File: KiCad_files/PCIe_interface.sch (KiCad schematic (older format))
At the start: 13 parts, among them J1 PCIe_x4_Connector, U1 XC7A35T_CSG325

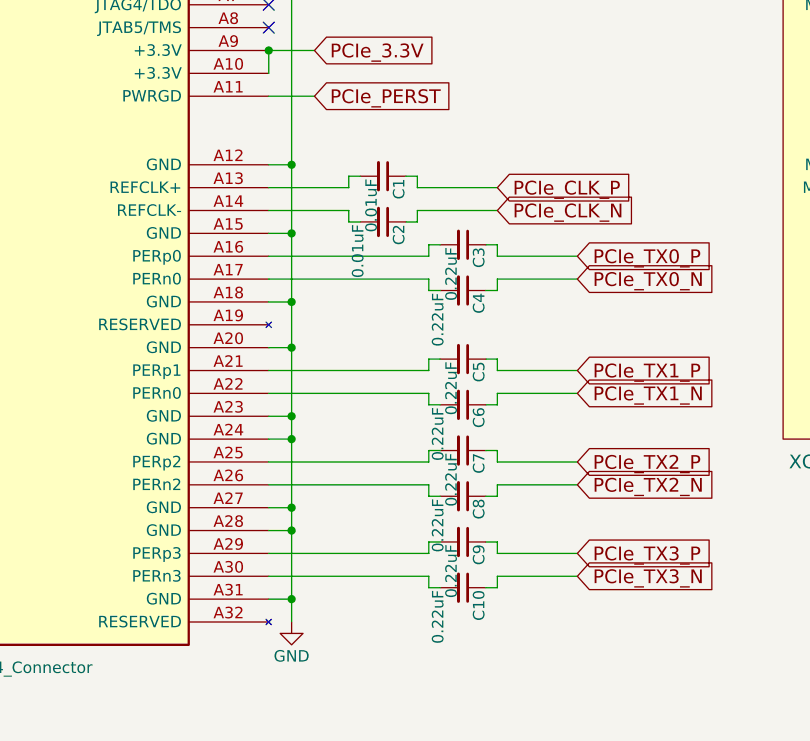
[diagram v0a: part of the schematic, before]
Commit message: Fixes during layout
Changed FT2232HL footprint to one with external pad
Made LGA123 (PI34XX) pins into blocks
Added labels for PCIe to let KiCad do differential pair routing
Removed some ground connections in SGND in PI34XX
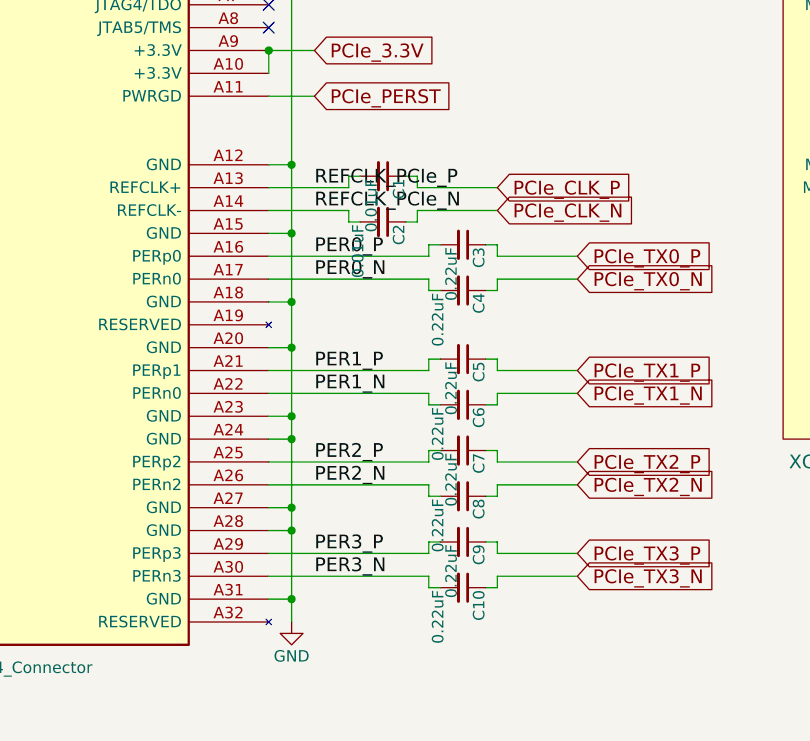
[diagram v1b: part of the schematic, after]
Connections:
- net REFCLK_PCIe_P: now reaches C1.2, J1.A13 (REFCLK+)
- net REFCLK_PCIe_N: now reaches C2.2, J1.A14 (REFCLK-)
- net PER0_P: now reaches C3.2, J1.A16 (PERp0)
- net PER0_N: now reaches C4.2, J1.A17 (PERn0)
- net PER1_P: now reaches C5.2, J1.A21 (PERp1)
- net PER1_N: now reaches C6.2, J1.A22 (PERn0)
- net PER2_P: now reaches C7.2, J1.A25 (PERp2)
- net PER2_N: now reaches C8.2, J1.A26 (PERn2)
- net PER3_P: now reaches C9.2, J1.A29 (PERp3)
- net PER3_N: now reaches C10.2, J1.A30 (PERn3)
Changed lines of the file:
@@
 	4300 6000 3800 6000
 NoConn ~ 2850 3900
+Text Label 5450 3500 0    60   ~ 0
+REFCLK_PCIe_P
+Text Label 5450 3600 0    60   ~ 0
+REFCLK_PCIe_N
+Text Label 5450 3800 0    60   ~ 0
+PER0_P
+Text Label 5450 3900 0    60   ~ 0
+PER0_N
+Text Label 5450 4300 0    60   ~ 0
+PER1_P
+Text Label 5450 4400 0    60   ~ 0
+PER1_N
+Text Label 5450 4700 0    60   ~ 0
+PER2_P
+Text Label 5450 4800 0    60   ~ 0
+PER2_N
+Text Label 5450 5100 0    60   ~ 0
+PER3_P
+Text Label 5450 5200 0    60   ~ 0
+PER3_N
 $EndSCHEMATC

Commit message: Purged RAM (SCH)
Was taking way too lon of a time which I didn't have
Also using larger resistors and capacitors than 0402 and 0201 (expect a very few)
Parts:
- C1, C2: footprint Capacitors_SMD:C_0402 -> Capacitors_SMD:C_1206
- C10, C3, C4, C5, C6, C7, C8, C9: footprint Capacitors_SMD:C_0402 -> Capacitors_SMD:C_0805
- R1: footprint Resistors_SMD:R_0402 -> Resistors_SMD:R_0603
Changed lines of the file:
@@
 $Descr A 11000 8500
 encoding utf-8
-Sheet 2 9
+Sheet 2 7
 Title "Reconfigurable Application-Specific Accelerator Card"
-Date "2019-02-27"
-Rev "1.0"
+Date "2019-03-31"
+Rev "0.9"
 Comp "Brian Hong & Jasmine Tang"
 Comment1 ""
@@
 F 0 "C1" H 5760 3520 50  0000 L CNN
 F 1 "0.01uF" H 5760 3370 50  0000 L BNN
-F 2 "Capacitors_SMD:C_0402" H 5750 3450 50  0001 C CNN
+F 2 "Capacitors_SMD:C_1206" H 5750 3450 50  0001 C CNN
 F 3 "" H 5750 3450 50  0001 C CNN
 	1    5750 3450
@@
 F 0 "C2" H 5760 3720 50  0000 L CNN
 F 1 "0.01uF" H 5760 3570 50  0000 L TNN
-F 2 "Capacitors_SMD:C_0402" H 5750 3650 50  0001 C CNN
+F 2 "Capacitors_SMD:C_1206" H 5750 3650 50  0001 C CNN
 F 3 "" H 5750 3650 50  0001 C CNN
 	1    5750 3650
@@
 F 0 "C3" H 6110 3820 50  0000 L CNN
 F 1 "0.22uF" H 6110 3670 50  0000 L BNN
-F 2 "Capacitors_SMD:C_0402" H 6100 3750 50  0001 C CNN
+F 2 "Capacitors_SMD:C_0805" H 6100 3750 50  0001 C CNN
 F 3 "" H 6100 3750 50  0001 C CNN
 	1    6100 3750
@@
 F 0 "C4" H 6110 4020 50  0000 L CNN
 F 1 "0.22uF" H 6110 3870 50  0000 L TNN
-F 2 "Capacitors_SMD:C_0402" H 6100 3950 50  0001 C CNN
+F 2 "Capacitors_SMD:C_0805" H 6100 3950 50  0001 C CNN
 F 3 "" H 6100 3950 50  0001 C CNN
 	1    6100 3950
@@
 F 0 "C5" H 6110 4320 50  0000 L CNN
 F 1 "0.22uF" H 6110 4170 50  0000 L BNN
-F 2 "Capacitors_SMD:C_0402" H 6100 4250 50  0001 C CNN
+F 2 "Capacitors_SMD:C_0805" H 6100 4250 50  0001 C CNN
 F 3 "" H 6100 4250 50  0001 C CNN
 	1    6100 4250
@@
 F 0 "C6" H 6110 4520 50  0000 L CNN
 F 1 "0.22uF" H 6110 4370 50  0000 L TNN
-F 2 "Capacitors_SMD:C_0402" H 6100 4450 50  0001 C CNN
+F 2 "Capacitors_SMD:C_0805" H 6100 4450 50  0001 C CNN
 F 3 "" H 6100 4450 50  0001 C CNN
 	1    6100 4450
@@
 F 0 "C7" H 6110 4720 50  0000 L CNN
 F 1 "0.22uF" H 6110 4570 50  0000 L BNN
-F 2 "Capacitors_SMD:C_0402" H 6100 4650 50  0001 C CNN
+F 2 "Capacitors_SMD:C_0805" H 6100 4650 50  0001 C CNN
 F 3 "" H 6100 4650 50  0001 C CNN
 	1    6100 4650
@@
 F 0 "C8" H 6110 4920 50  0000 L CNN
 F 1 "0.22uF" H 6110 4770 50  0000 L TNN
-F 2 "Capacitors_SMD:C_0402" H 6100 4850 50  0001 C CNN
+F 2 "Capacitors_SMD:C_0805" H 6100 4850 50  0001 C CNN
 F 3 "" H 6100 4850 50  0001 C CNN
 	1    6100 4850
@@
 F 0 "C9" H 6110 5120 50  0000 L CNN
 F 1 "0.22uF" H 6110 4970 50  0000 L BNN
-F 2 "Capacitors_SMD:C_0402" H 6100 5050 50  0001 C CNN
+F 2 "Capacitors_SMD:C_0805" H 6100 5050 50  0001 C CNN
 F 3 "" H 6100 5050 50  0001 C CNN
 	1    6100 5050
@@
 F 0 "C10" H 6110 5320 50  0000 L CNN
 F 1 "0.22uF" H 6110 5170 50  0000 L TNN
-F 2 "Capacitors_SMD:C_0402" H 6100 5250 50  0001 C CNN
+F 2 "Capacitors_SMD:C_0805" H 6100 5250 50  0001 C CNN
 F 3 "" H 6100 5250 50  0001 C CNN
 	1    6100 5250
@@
 F 0 "R1" V 8730 2500 50  0000 C CNN
 F 1 "100" V 8650 2500 50  0000 C CNN
-F 2 "Resistors_SMD:R_0402" V 8580 2500 50  0001 C CNN
+F 2 "Resistors_SMD:R_0603" V 8580 2500 50  0001 C CNN
 F 3 "" H 8650 2500 50  0001 C CNN
 	1    8650 2500
